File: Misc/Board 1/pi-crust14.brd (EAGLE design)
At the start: 101.6 x 78.8 mm, 40 parts, among them IC10 40193N, IC2 74LS595D, IC3 74LS595D, IC4 74LS595D, IC5 74LS595D, IC6 74LS595D, IC7 74LS595D, IC8 74AC11008, U1 AD9983AKSTZ_140, U2 SN54LS253_J_16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

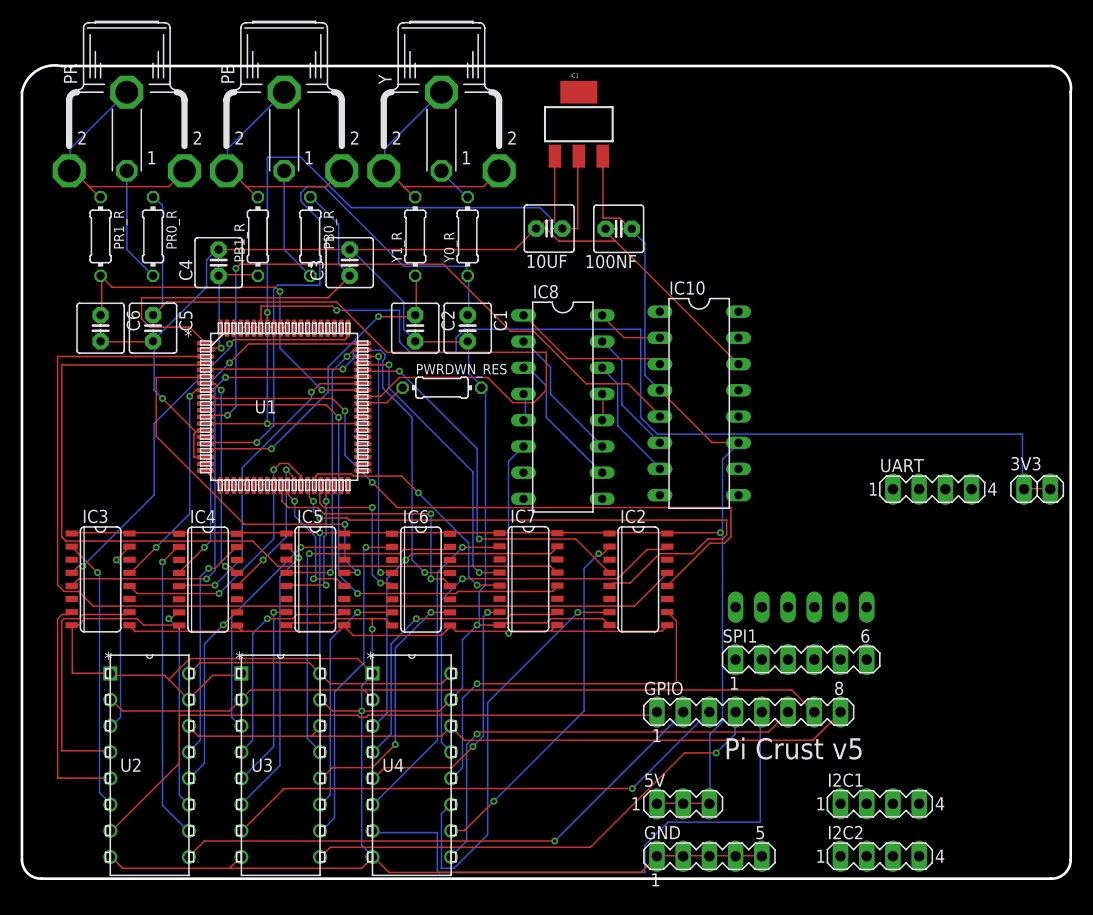
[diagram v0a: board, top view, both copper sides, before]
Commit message: Board Update 4
Update to 1.8V Power Supply, ADC updates, still need ADC finalization as
well as RCA replacement
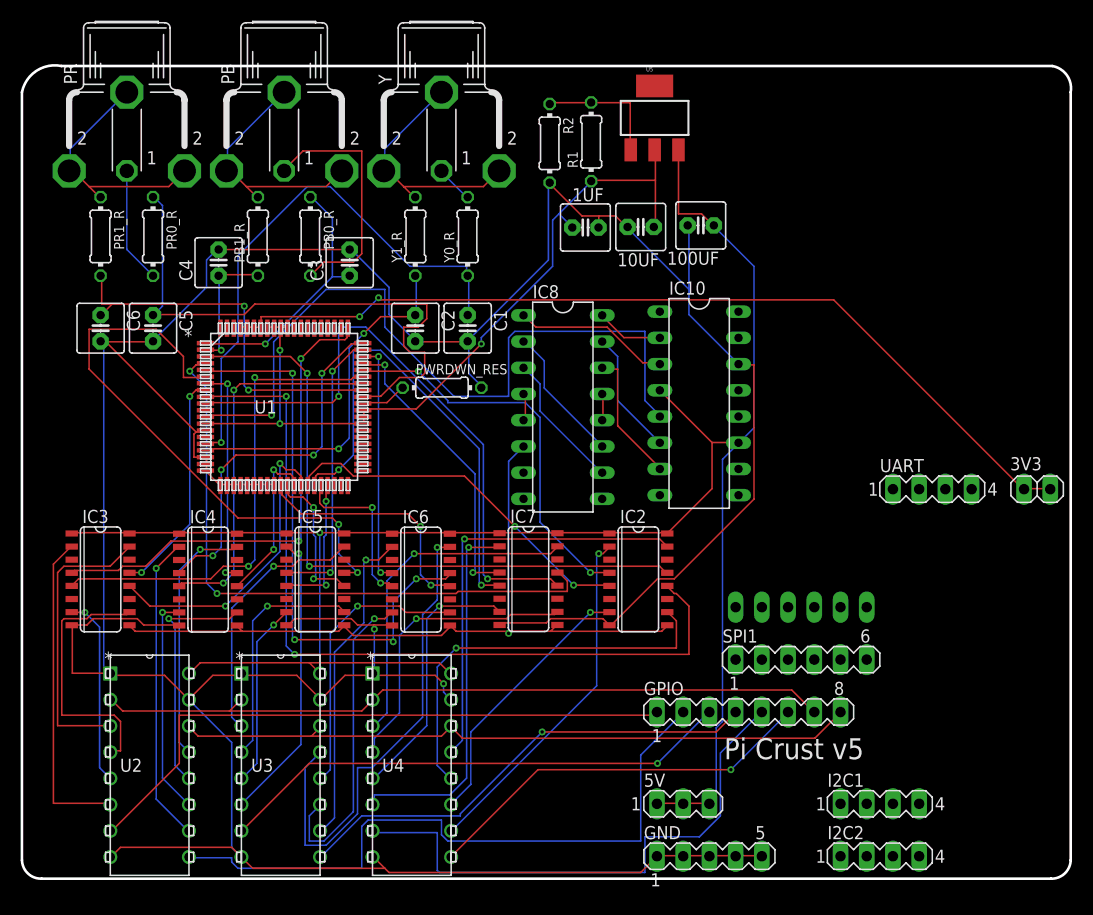
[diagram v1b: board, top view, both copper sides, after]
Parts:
- removed 100NF: (no value), capacitor-wima:C2.5-5
- removed IC1: (no value), SparkFun-PowerIC:SOT223
- added .1UF, 100UF: (no value), capacitor-wima:C2.5-5
- added R1: 240, rcl:0204/7
- added R2: 105, rcl:0204/7
- added U5: V_REG_317SMD, SparkFun-PowerIC:SOT223
- moved 10UF 8.87 mm to (59.9, 63.1)
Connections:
- new net U1: R1.2, R2.1, U5.1
- net 1.8V: now also .1UF.1, R1.1, U5.2; no longer IC1.2
- net 5V: now also 100UF.1, U5.3; no longer 100NF.1, IC1.3
- net GND_WIRE: now also .1UF.2, 100UF.2, R2.2; no longer 100NF.2, IC1.1
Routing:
- net B0: track 97.7 -> 64.2 mm, vias 0 -> 2
- net G4: track 58.0 -> 35.5 mm
- net G5: track 25.3 -> 46.9 mm
- net GND_WIRE: track 345.8 -> 366.8 mm, vias 4 -> 2
- net RIN0_ADC: track 76.6 -> 56.3 mm
- net B1: track 80.1 -> 60.8 mm, vias 0 -> 2
- net B3: track 38.8 -> 55.4 mm
- net G4_OUT: track 40.6 -> 26.1 mm
- net U1: track 0.00 -> 14.2 mm
- net BIN0_ADC: track 39.5 -> 25.4 mm, vias 0 -> 1
- net 5V: track 181.6 -> 195.4 mm, vias 2 -> 1
- net B2_OUT: track 33.7 -> 47.1 mm
- net PBIN_0: track 11.2 -> 24.2 mm
- net 3V3: track 100.7 -> 88.2 mm, vias 1 -> 2
- net MSB2: track 53.7 -> 64.6 mm, vias 1 -> 0
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
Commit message: Board Update 4
Email sent to CUI for RCA Eagle File, RPI 2 female pins added to board,
ADC pins configured
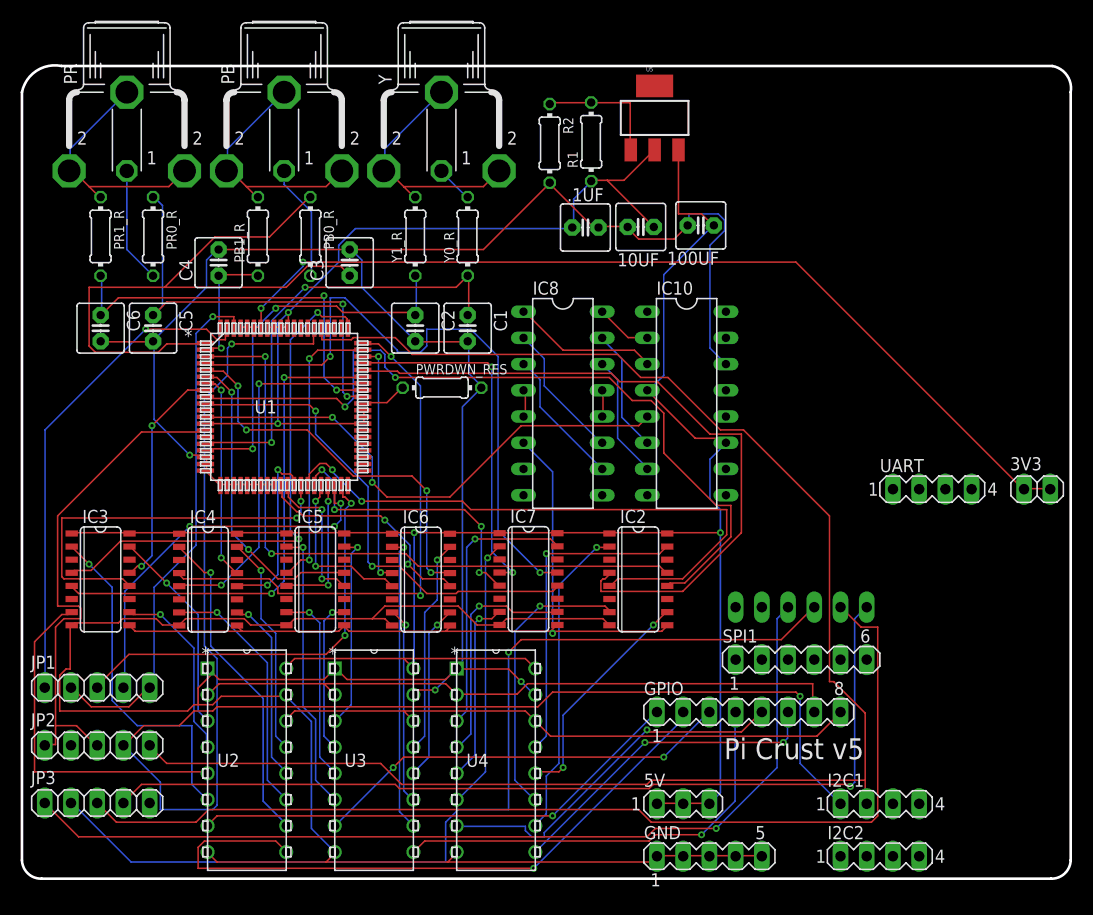
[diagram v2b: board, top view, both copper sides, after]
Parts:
- added JP1, JP2, JP3: (no value), pinhead:1X05
- moved U2 9.44 mm to (25.6, 2.59)
- moved U3 9.06 mm to (37.9, 2.59)
- moved U4 8.17 mm to (49.7, 2.59)
- moved IC10 1.22 mm to (64.4, 46.1)
- moved IC8 0.36 mm to (52.4, 46.1)
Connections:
- new net CE: JP3.1, SPI0.4
- new net CLAMP: JP2.2
- new net EXTCLK/COAST: JP2.1, JP2.3, U1.72
- new net HSOUT: JP1.4, U1.23
- new net HSYNC0: JP1.3, U1.70
- new net MISO: JP3.3, SPI0.2
- new net MOSI: JP3.2, SPI0.3
- new net SCL: I2C1.2, JP2.5, U1.67
- new net SCLK: JP3.4, SPI0.1
- new net SDA: I2C1.1, JP2.4, U1.66
- new net VSOUT/A0: JP1.2, JP1.5, U1.22
- new net VSYNC0: JP1.1, U1.71
- net GND_WIRE: no longer U1.72
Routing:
- net SCL: track 0.00 -> 158.3 mm
- net SDA: track 0.00 -> 149.0 mm, vias 0 -> 2
- net MISO: track 0.00 -> 100.3 mm
- net MOSI: track 0.00 -> 95.8 mm, vias 0 -> 1
- net CE: track 0.00 -> 91.1 mm, vias 0 -> 1
- net SCLK: track 0.00 -> 89.7 mm, vias 0 -> 1
- net VSOUT/A0: track 0.00 -> 50.8 mm, vias 0 -> 1
- net EXTCLK/COAST: track 0.00 -> 49.9 mm
- net VSYNC0: track 0.00 -> 48.1 mm, vias 0 -> 1
- net HSYNC0: track 0.00 -> 41.5 mm, vias 0 -> 2
- net HSOUT: track 0.00 -> 37.1 mm, vias 0 -> 3
- net BIN0_ADC: track 25.4 -> 61.8 mm, vias 1 -> 0
- net R2: track 38.1 -> 67.0 mm, vias 2 -> 0
- net B2_OUT: track 47.1 -> 20.9 mm
- net B3: track 55.4 -> 29.8 mm
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
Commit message: Board Update 5
RCA and Filter still incorrect, all other functions verified and correct
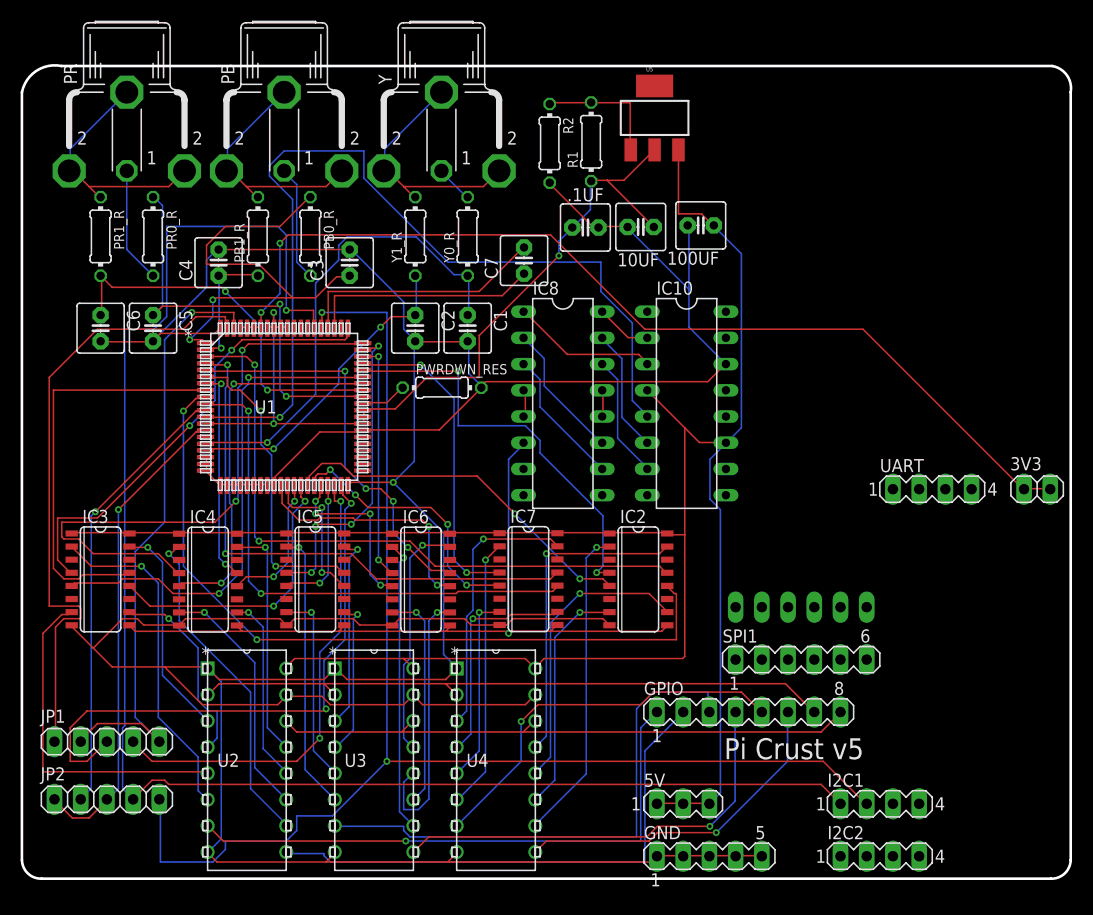
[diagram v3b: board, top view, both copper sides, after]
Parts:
- removed JP3: (no value), pinhead:1X05
- added C7: 10u, capacitor-wima:C2.5-5
- moved JP1 5.32 mm to (8.23, 13.3)
- moved JP2 5.32 mm to (8.23, 7.70)
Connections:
- removed net CE: JP3.1, SPI0.4
- removed net MISO: JP3.3, SPI0.2
- removed net MOSI: JP3.2, SPI0.3
- removed net SCLK: JP3.4, SPI0.1
- new net FILT: U1.78
- new net REFHI: C7.1, U1.20
- new net REFLO: C7.2, U1.18
- net CLAMP: now also U1.73
- net GND_WIRE: now also U1.21, U1.68, U1.69
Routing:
- net MISO: track 100.3 -> 0.00 mm
- net MOSI: track 95.8 -> 0.00 mm, vias 1 -> 0
- net CE: track 91.1 -> 0.00 mm, vias 1 -> 0
- net SCLK: track 89.7 -> 0.00 mm, vias 1 -> 0
- net CLAMP: track 0.00 -> 43.2 mm, vias 0 -> 1
- net DATACLK: track 50.7 -> 88.6 mm, vias 2 -> 1
- net GND_WIRE: track 369.0 -> 399.7 mm, vias 3 -> 1
- net R2: track 67.0 -> 39.9 mm, vias 0 -> 2
- net SCL: track 158.3 -> 132.9 mm, vias 0 -> 2
- net 5V: track 183.4 -> 208.0 mm, vias 2 -> 0
- net G4: track 59.9 -> 35.5 mm
- net REFLO: track 0.00 -> 24.3 mm
- net REFHI: track 0.00 -> 22.4 mm
- net B5: track 22.1 -> 40.1 mm, vias 2 -> 0
- net BIN0_ADC: track 61.8 -> 44.2 mm, vias 0 -> 2
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
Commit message: Board Update 6
RCA and wire size still incorrect (everything else complete), Filter
added, ADC correct, Removal of unnecessary wires
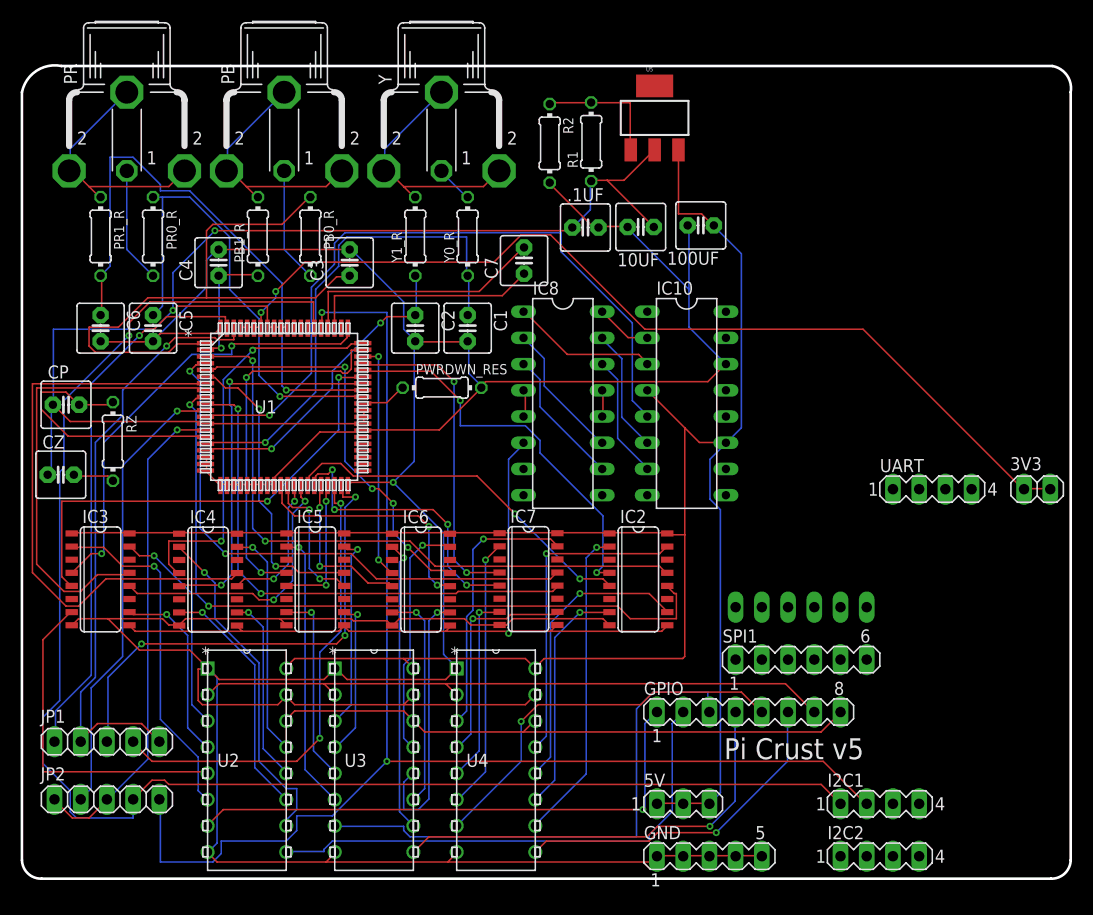
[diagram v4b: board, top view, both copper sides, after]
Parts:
- added CP: 8.2nF, capacitor-wima:C2.5-5
- added CZ: 82nF, capacitor-wima:C2.5-5
- added RZ: 1.5k, eagle-ltspice:0204/7
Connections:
- new net N$1: CZ.2, RZ.2
- net 1.8V: now also CP.1, CZ.1
- net FILT: now also CP.2, RZ.1
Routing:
- net 1.8V: track 81.1 -> 135.9 mm, vias 3 -> 2
- net B4: track 20.8 -> 57.6 mm, vias 2 -> 0
- net FILT: track 0.00 -> 26.3 mm
- net R6: track 58.8 -> 39.4 mm
- net DATACLK: track 88.6 -> 69.2 mm
- net RIN1_ADC: track 37.0 -> 55.8 mm, vias 2 -> 1
- net BIN0_ADC: track 44.2 -> 59.0 mm, vias 2 -> 0
- net HSYNC0: track 56.4 -> 47.2 mm, vias 2 -> 3
- net VSYNC0: track 60.9 -> 53.0 mm, vias 0 -> 1
- net R5: track 30.7 -> 35.6 mm, vias 4 -> 2
- net RIN0_ADC: track 41.6 -> 46.3 mm, vias 2 -> 1
- net B5: track 40.1 -> 44.4 mm
- net N$1: track 0.00 -> 4.05 mm
- net MSB1: track 55.7 -> 52.9 mm
- net R1: track 48.4 -> 45.8 mm
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
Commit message: Board Update 7
Rather than using the TOBU3, I have used a 1x1 pin header and used the
dimensions of RCJ-32265 (our RCA jack).  I also had to move some
resistors and capacitors around because of the order of input.  All else
remains the same as in 14
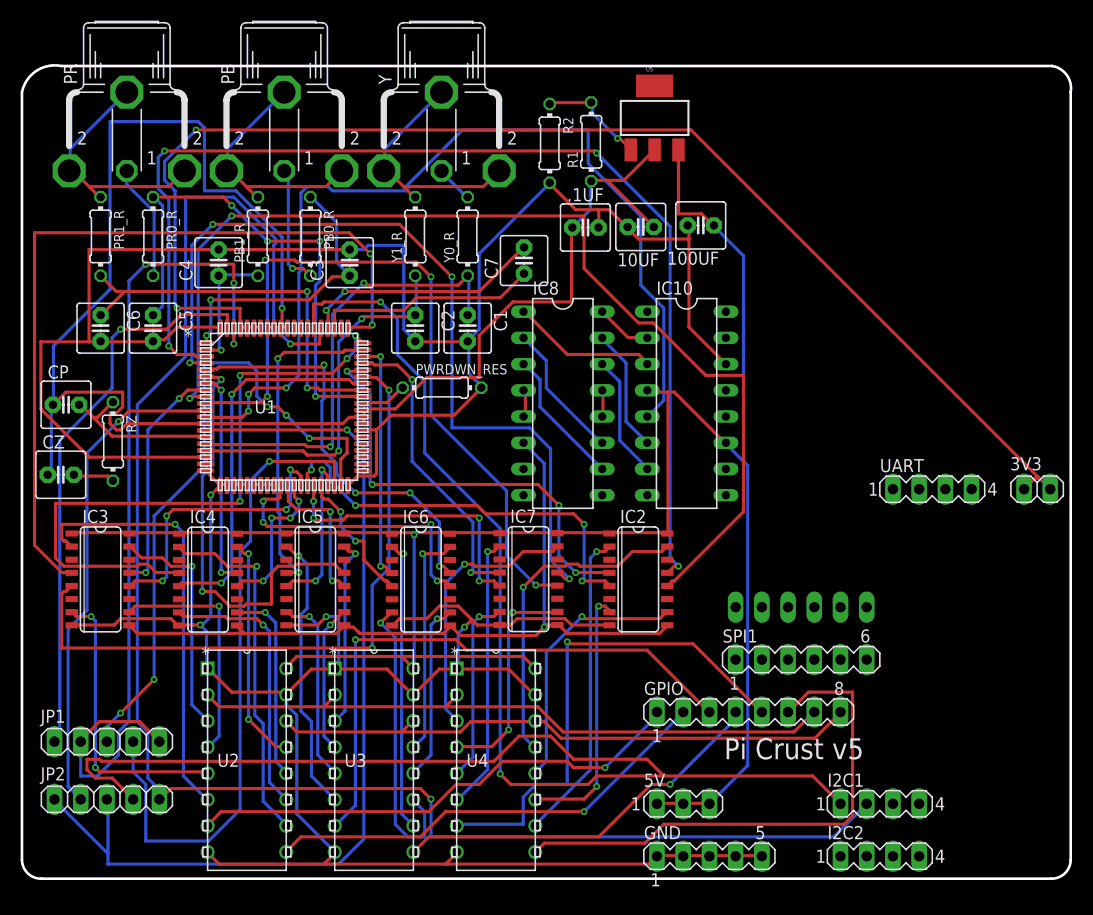
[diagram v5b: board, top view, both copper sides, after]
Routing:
- net B0: track 62.9 -> 110.1 mm, vias 2 -> 4
- net EXTCLK/COAST: track 48.0 -> 93.5 mm
- net B4: track 57.6 -> 21.0 mm, vias 0 -> 2
- net 3V3: track 93.9 -> 128.3 mm
- net R7: track 43.7 -> 77.8 mm
- net B6: track 71.6 -> 103.5 mm
- net GND_WIRE: track 397.5 -> 366.4 mm, vias 1 -> 4
- net BIN0_ADC: track 59.0 -> 28.1 mm, vias 0 -> 2
- net SCL: track 133.1 -> 161.3 mm
- net 1.8V: track 135.9 -> 163.9 mm, vias 2 -> 1
- net B1: track 54.4 -> 80.9 mm, vias 2 -> 4
- net VSOUT/A0: track 59.0 -> 83.6 mm, vias 1 -> 3
- net R6: track 39.4 -> 62.8 mm, vias 2 -> 4
- net DATACLK: track 69.2 -> 92.0 mm, vias 1 -> 3
- net B5: track 44.4 -> 22.7 mm, vias 0 -> 2
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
